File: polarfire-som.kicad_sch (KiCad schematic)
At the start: 12 parts

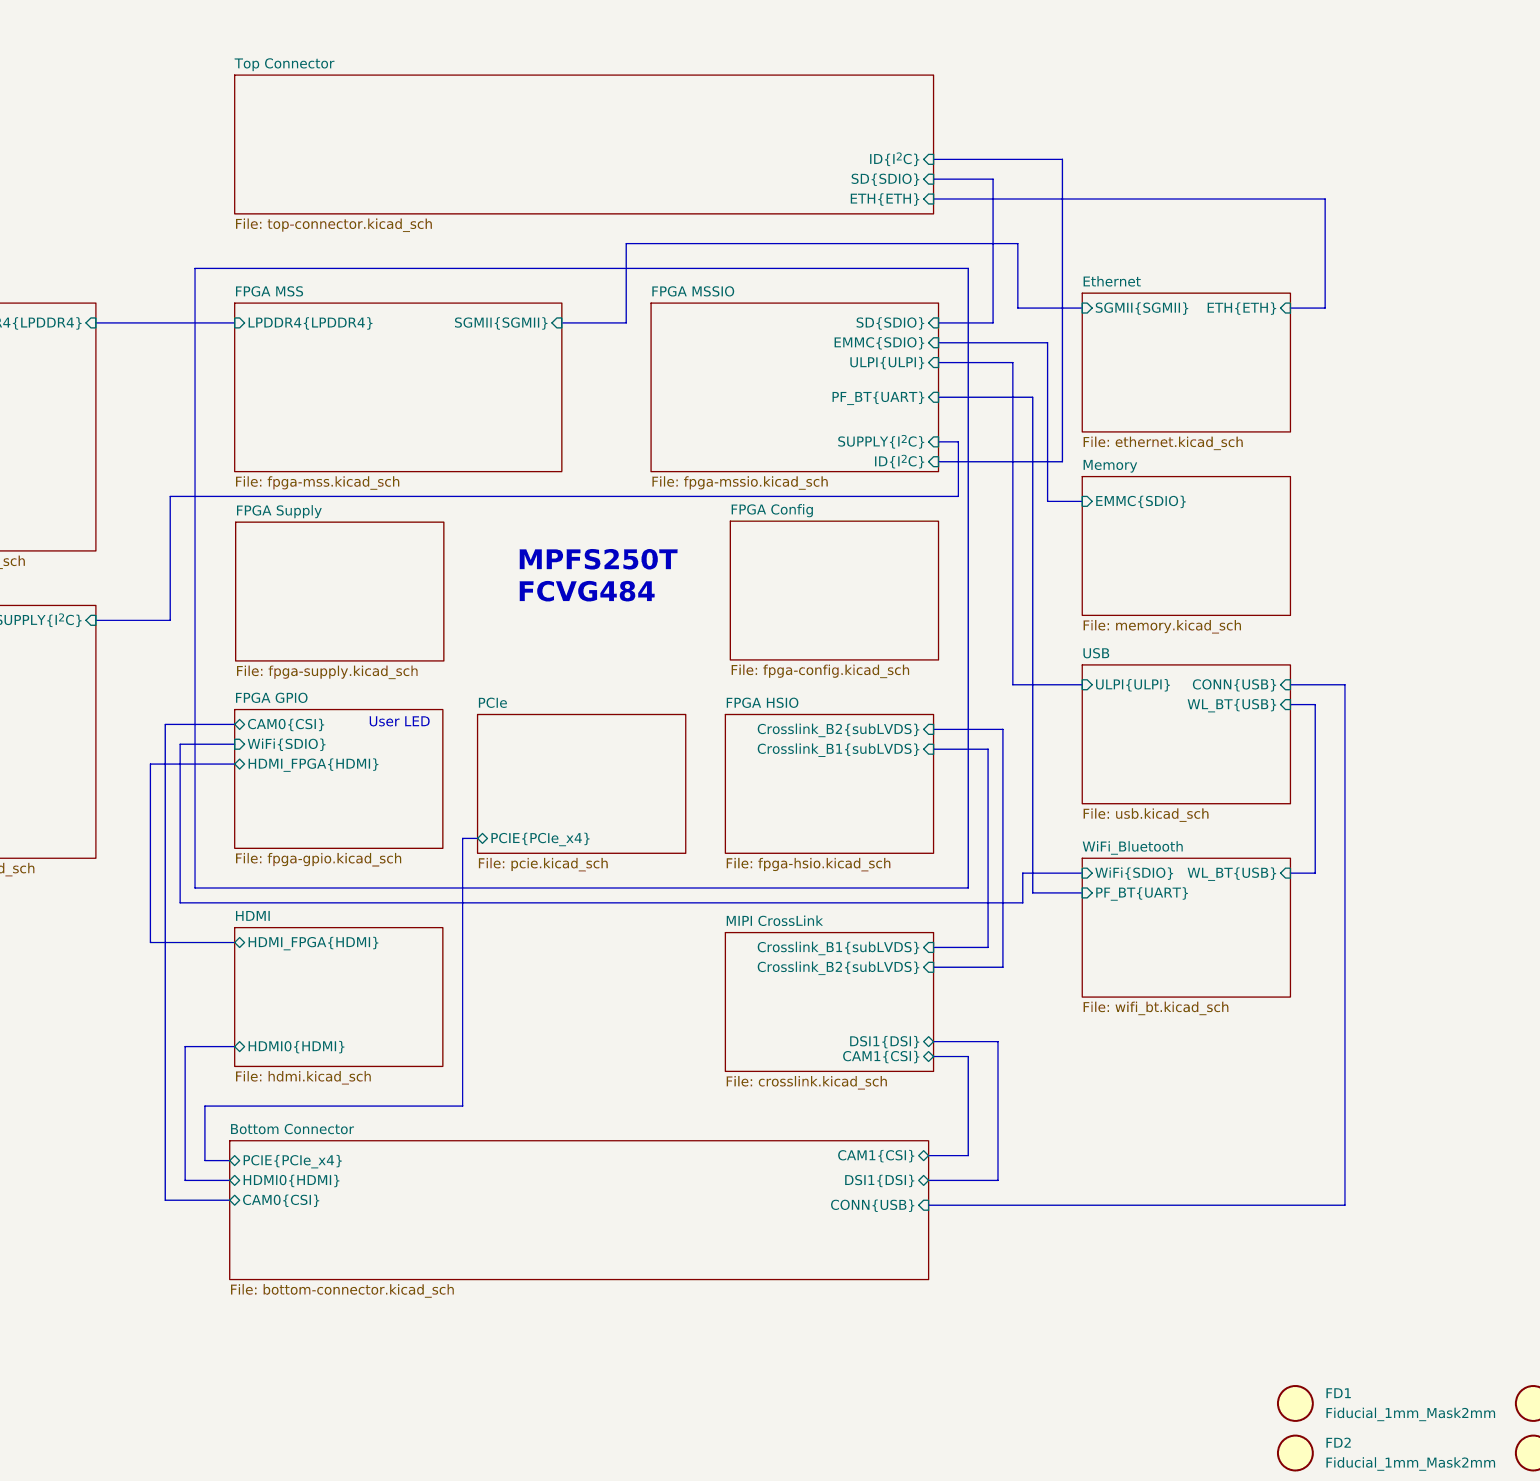
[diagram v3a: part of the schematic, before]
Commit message: [#57505] Start moving logic level converters to GPIO sheet
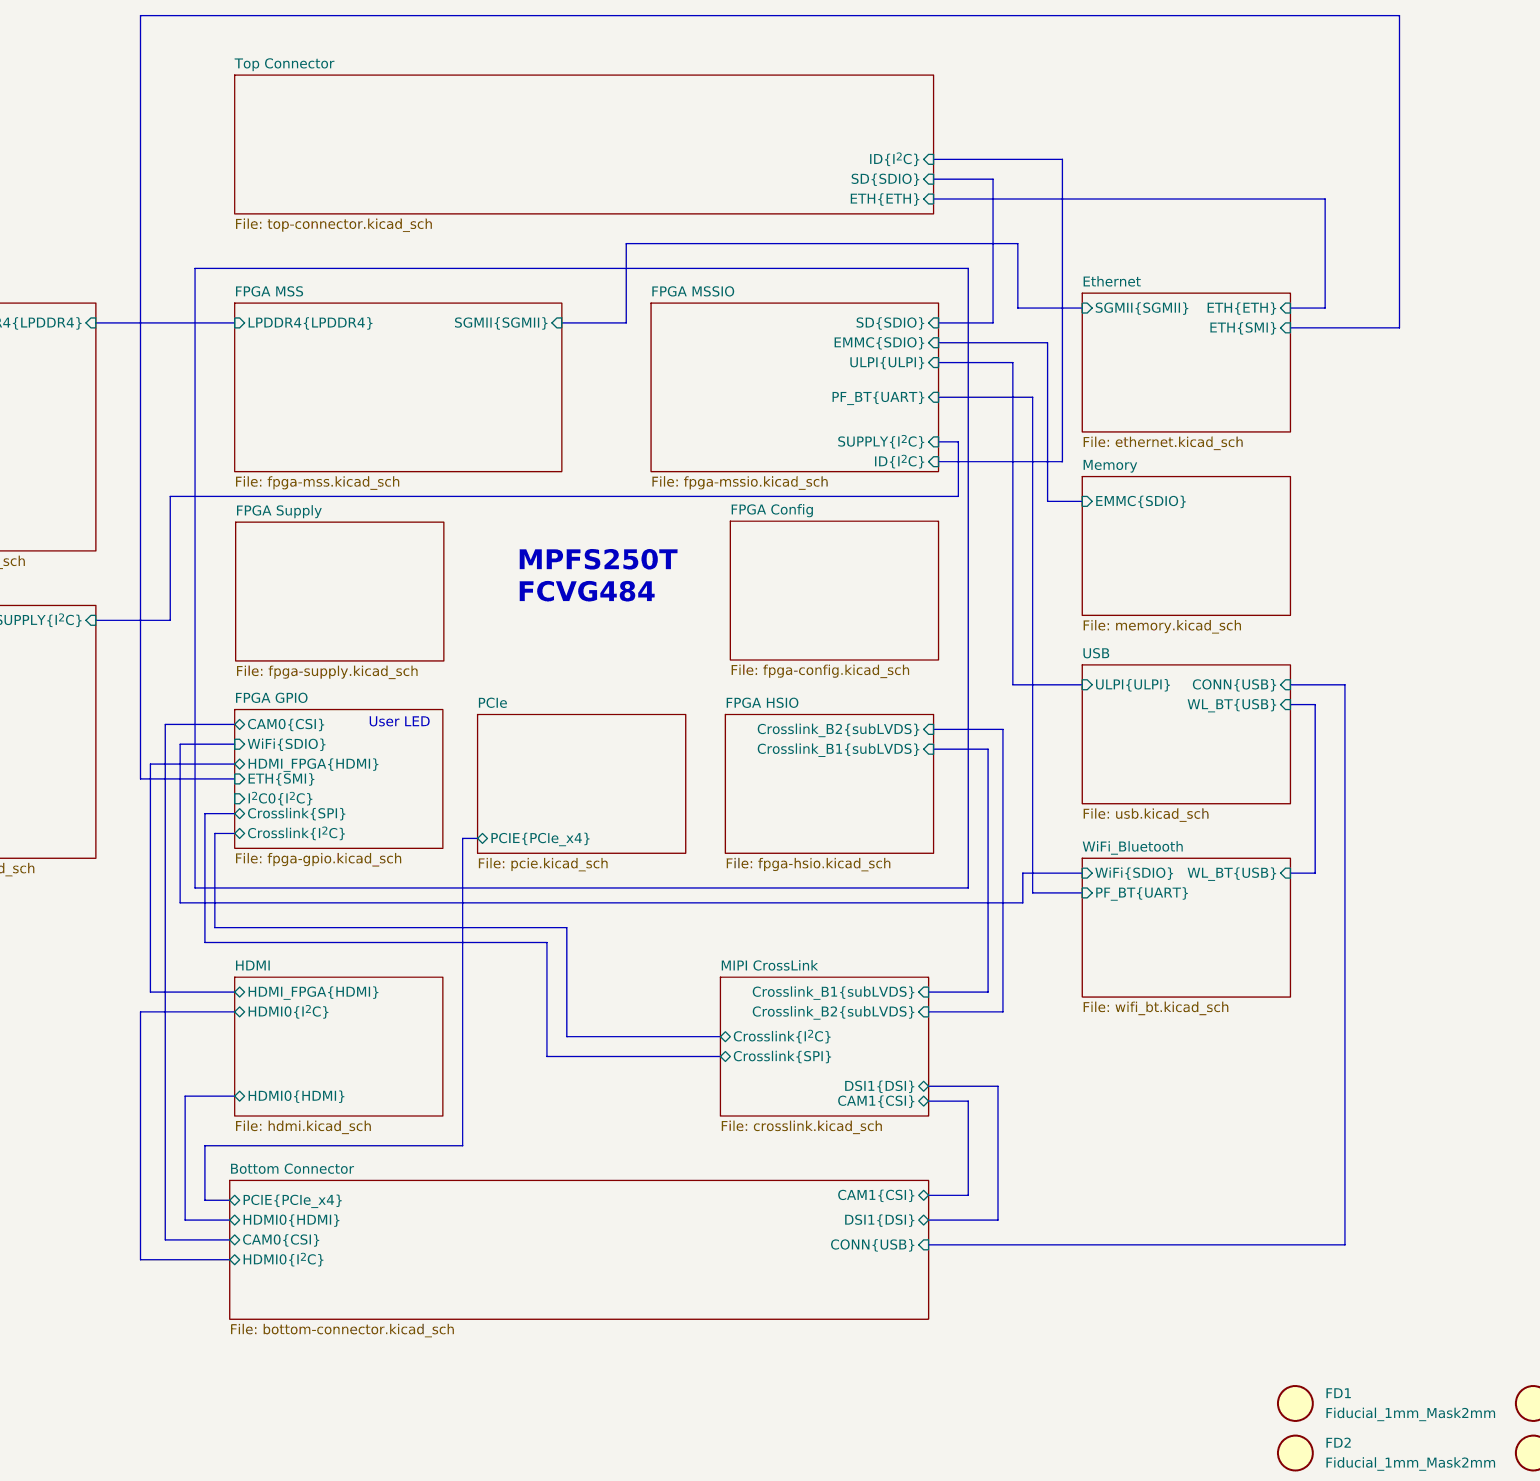
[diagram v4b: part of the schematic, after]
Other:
- sheet Bottom Connector ports: added HDMI0{I^{2}C}; removed none
- sheet Ethernet ports: added ETH{SMI}; removed none
- sheet FPGA GPIO ports: added Crosslink{I^{2}C}, Crosslink{SPI}, ETH{SMI}, I^{2}C0{I^{2}C}; removed none
- sheet HDMI ports: added HDMI0{I^{2}C}; removed none
- sheet MIPI CrossLink ports: added Crosslink{I^{2}C}, Crosslink{SPI}; removed none

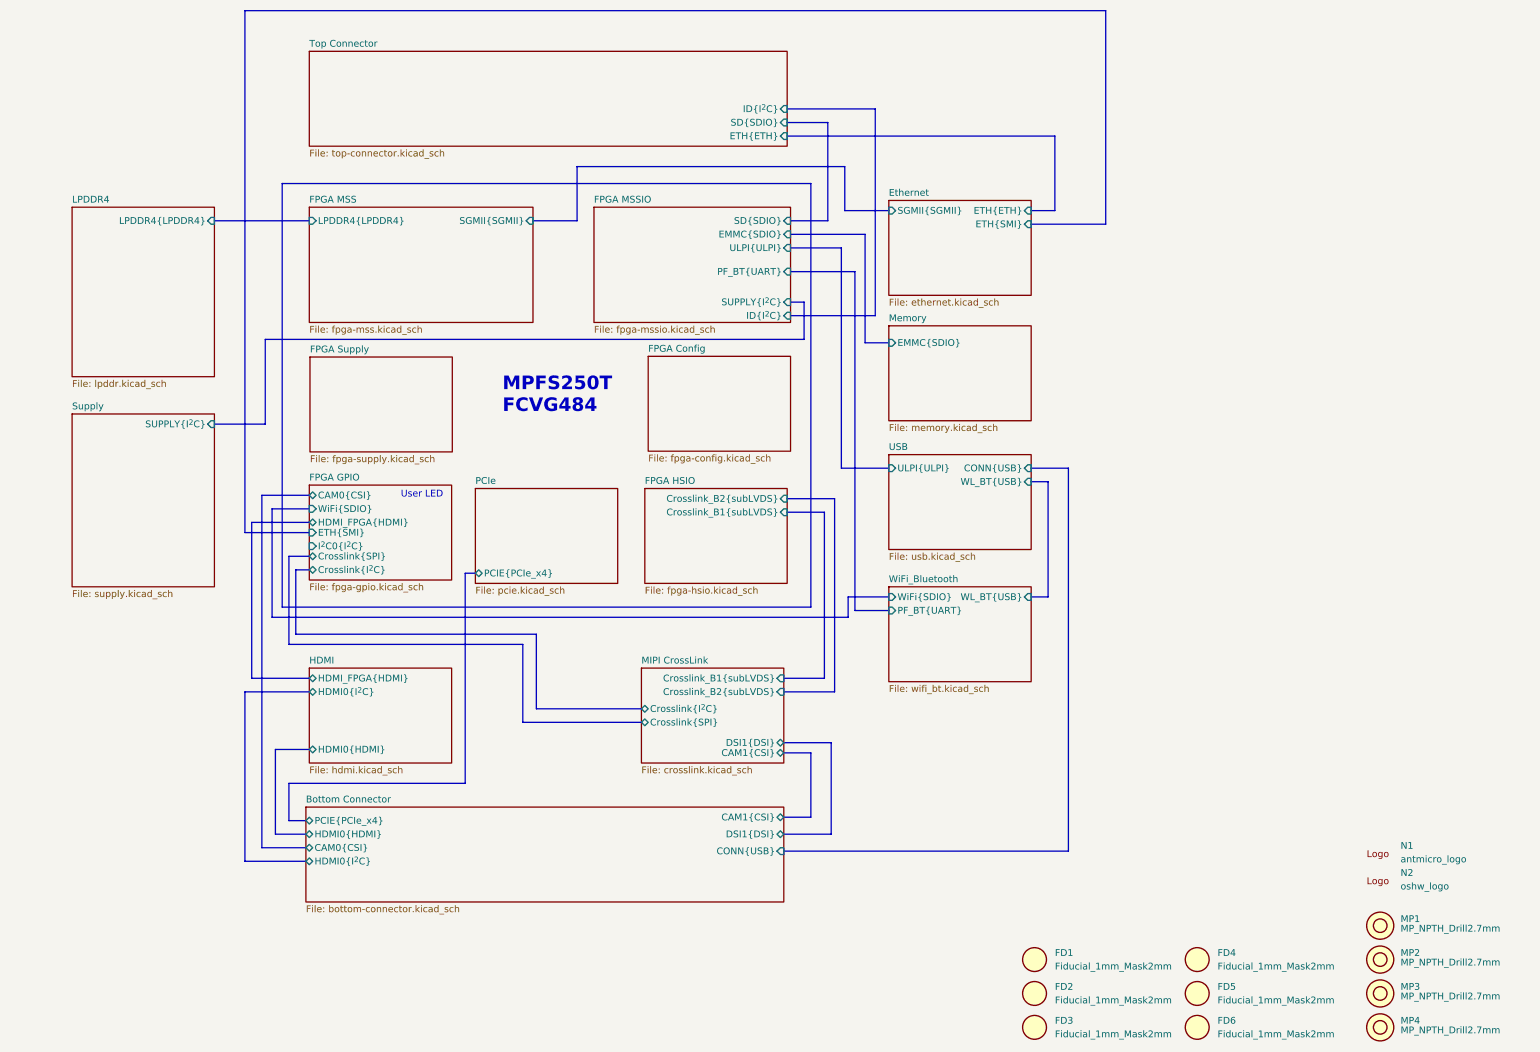
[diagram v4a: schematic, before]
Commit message: [#57505] Finish migration to hierarchical structure
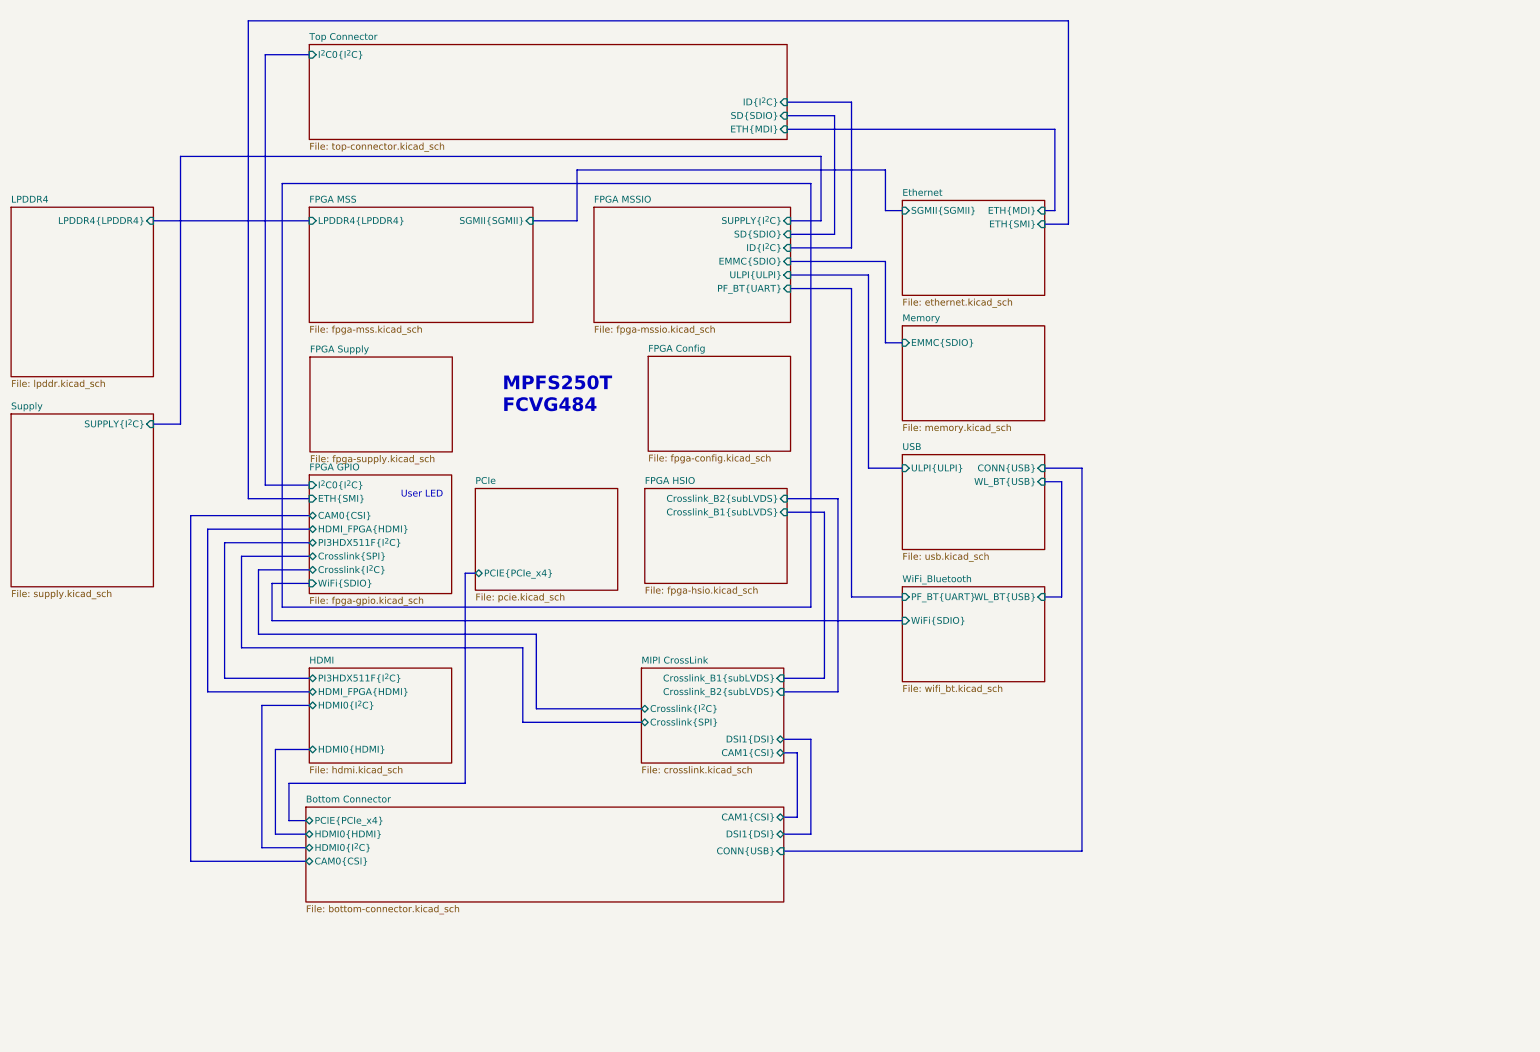
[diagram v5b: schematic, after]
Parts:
- removed FD1, FD2, FD3, FD4, FD5, FD6: Fiducial_1mm_Mask2mm, antmicro-footprints:Fiducial_1mm_Mask2mm, symbol antmicroFiducialMarks:Fiducial_1mm_Mask2mm
- removed MP1, MP2, MP3, MP4: MP_NPTH_Drill2.7mm, antmicro-footprints:MP_NPTH_Drill2.7mm, symbol antmicroMechanicalParts:MP_NPTH_Drill2.7mm
- removed N1: antmicro_logo, antmicro-footprints:antmicro-logo_scaled_12mm_silk, symbol antmicroMechanicalParts:antmicro_logo
- removed N2: oshw_logo, antmicro-footprints:OSHW-Logo_5.7x6mm_SilkScreen, symbol antmicroMechanicalParts:oshw_logo
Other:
- sheet Ethernet ports: added ETH{MDI}; removed ETH{ETH}
- sheet FPGA GPIO ports: added PI3HDX511F{I^{2}C}; removed none
- sheet HDMI ports: added PI3HDX511F{I^{2}C}; removed none
- sheet Top Connector ports: added ETH{MDI}, I^{2}C0{I^{2}C}; removed ETH{ETH}

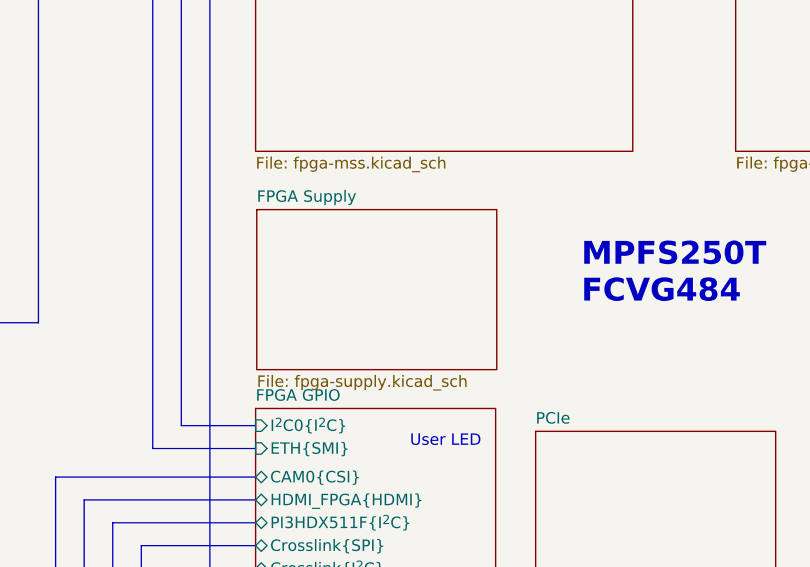
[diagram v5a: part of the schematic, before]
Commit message: [#57422] Clean DRC
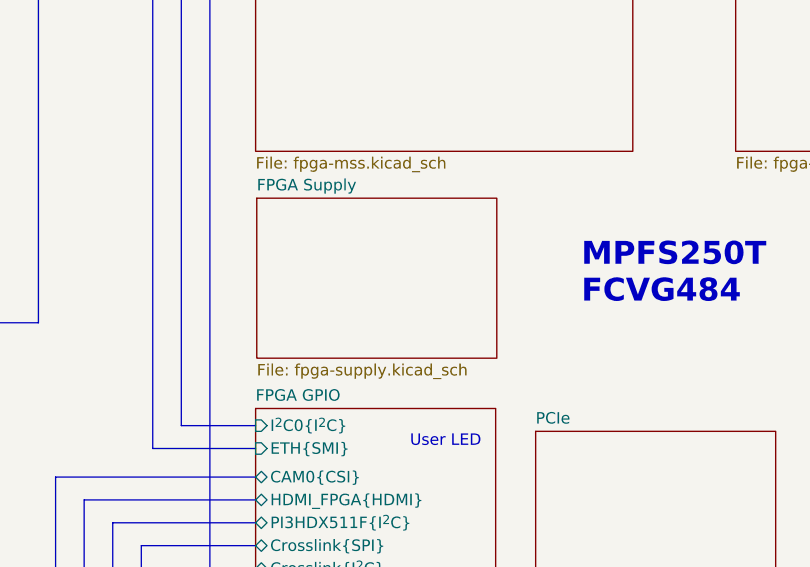
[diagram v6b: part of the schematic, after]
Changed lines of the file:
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@@
     )
   )
-  (sheet (at 172.847 116.967) (size 26.67 17.78) (fields_autoplaced)
+  (sheet (at 172.847 115.697) (size 26.67 17.78) (fields_autoplaced)
     (stroke (width 0.1524) (type solid))
     (fill (color 0 0 0 0.0000))
-    (property "Sheetname" "FPGA Supply" (at 172.847 116.2554 0)
+    (property "Sheetname" "FPGA Supply" (at 172.847 114.9854 0)
       (effects (font (size 1.27 1.27)) (justify left bottom))
     )
-    (property "Sheetfile" "fpga-supply.kicad_sch" (at 172.847 135.3316 0)
+    (property "Sheetfile" "fpga-supply.kicad_sch" (at 172.847 134.0616 0)
       (effects (font (size 1.27 1.27)) (justify left top))
     )

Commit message: [#57422] Finishing touches
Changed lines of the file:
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@@
   (title_block
     (title "PolarFire SoM")
-    (date "2024-04-03")
+    (date "2024-04-08")
     (rev "1.0.0")
     (company "Antmicro Ltd")
@@
   )
   (polyline (pts (xy 266.7 163.83) (xy 167.64 163.83))
-    (stroke (width 0) (type default))
+    (stroke (width 0) (type dash))
   )
   (bus (pts (xy 262.89 91.44) (xy 268.605 91.44))
@@
   )
   (polyline (pts (xy 266.7 84.455) (xy 266.7 163.83))
-    (stroke (width 0) (type default))
+    (stroke (width 0) (type dash))
   )
   (bus (pts (xy 212.725 185.42) (xy 234.95 185.42))
@@
   )
   (polyline (pts (xy 167.64 84.455) (xy 266.7 84.455))
-    (stroke (width 0) (type default))
+    (stroke (width 0) (type dash))
   )
   (bus (pts (xy 172.085 211.455) (xy 150.495 211.455))
@@
   )
   (polyline (pts (xy 167.64 163.83) (xy 167.64 84.455))
-    (stroke (width 0) (type default))
+    (stroke (width 0) (type dash))
   )
   (bus (pts (xy 214.63 91.44) (xy 222.885 91.44))
